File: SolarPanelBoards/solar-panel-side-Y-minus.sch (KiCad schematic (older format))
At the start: 24 parts, among them J1 Conn_01x06, U1 OPT3001DNPT

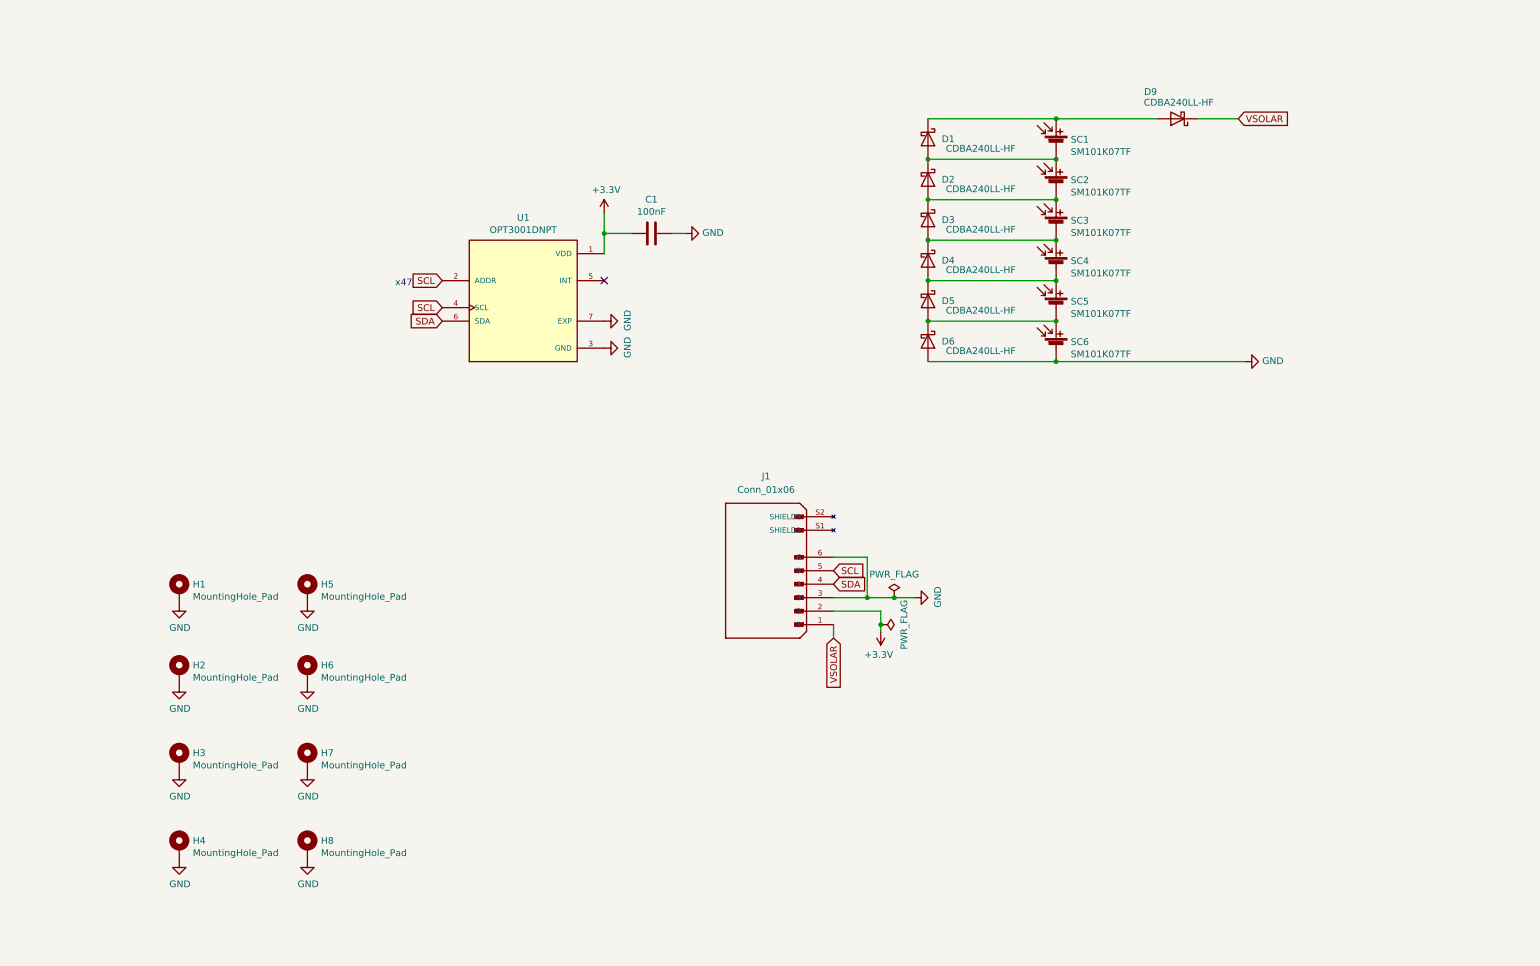
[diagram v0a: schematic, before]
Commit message: Battery board and side panels ready for CAD check and review, pycubed not finished yet
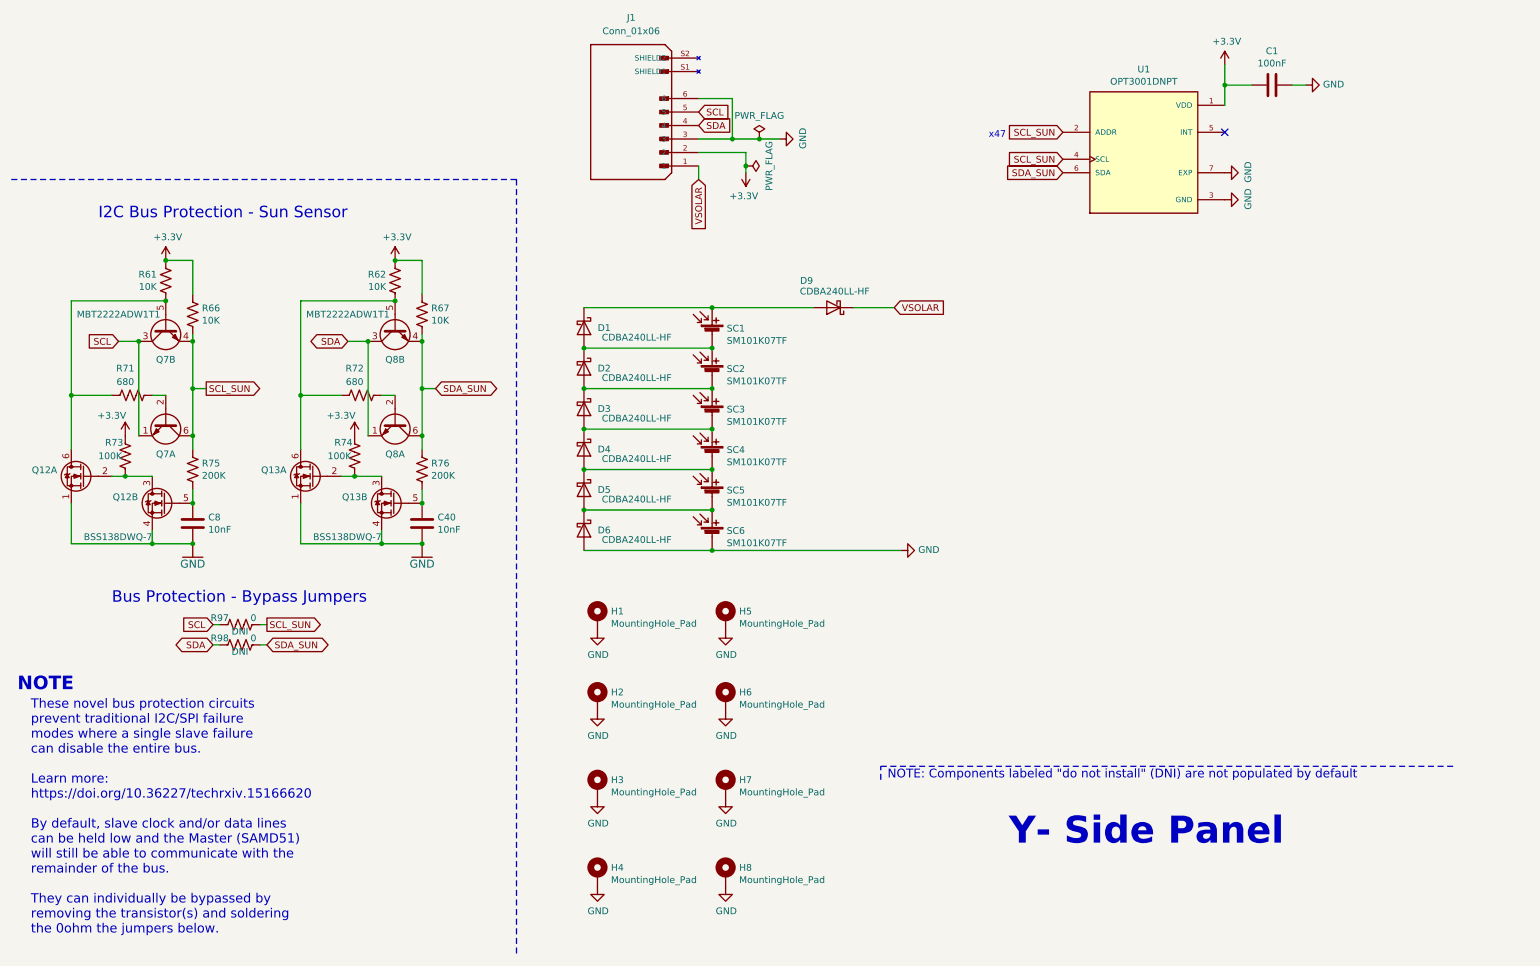
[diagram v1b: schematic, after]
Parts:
- added C40, C8: 10nF, Capacitor_SMD:C_0603_1608Metric, symbol Device:C
- added Q12, Q13: BSS138DWQ-7, sapling:BSS138DWQ-7, symbol mainboard:BSS138DWQ-7
- added Q7, Q8: MBT2222ADW1T1, Package_TO_SOT_SMD:SOT-363_SC-70-6, symbol Transistor_BJT:MBT2222ADW1T1
- added R61, R62, R66, R67: 10K, Resistor_SMD:R_0603_1608Metric, symbol Device:R_US
- added R71, R72: 680, Resistor_SMD:R_0603_1608Metric, symbol Device:R_US
- added R73, R74: 100K, Resistor_SMD:R_0603_1608Metric, symbol Device:R_US
- added R75, R76: 200K, Resistor_SMD:R_0603_1608Metric, symbol Device:R_US
- added R97, R98: 0, Resistor_SMD:R_0603_1608Metric, symbol Device:R_US
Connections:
- net +3V3: now also R61.1, R62.1, R66.1, R67.1, R73.1, R74.1
- net SCL: now also Q7.1 (E1), Q7.3 (C2), R97.2; no longer U1.2 (ADDR), U1.4 (SCL)
- net SDA: now also Q8.1 (E1), Q8.3 (C2), R98.2; no longer U1.6 (SDA)
- new net: C8.2, Q12.1 (S2), Q12.4 (S1)
- new net: Q12.2 (G2), Q12.3 (D2), R73.2
- new net: Q12.6 (D1), Q7.5 (B2), R61.2, R71.2
- new net: C8.1, Q12.5 (G1), R75.2
- new net: Q7.2 (B1), R71.1
- new net: Q8.2 (B1), R72.1
- new net: Q13.6 (D1), Q8.5 (B2), R62.2, R72.2
- new net: C40.1, Q13.5 (G1), R76.2
- new net: C40.2, Q13.1 (S2), Q13.4 (S1)
- new net: Q13.2 (G2), Q13.3 (D2), R74.2
- new net SCL_SUN: Q7.4 (E2), Q7.6 (C1), R66.2, R75.1, R97.1, U1.2 (ADDR), U1.4 (SCL)
- new net SDA_SUN: Q8.4 (E2), Q8.6 (C1), R67.2, R76.1, R98.1, U1.6 (SDA)
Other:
- note added: "Bus Protection - Bypass Jumpers"
- note added: "I2C Bus Protection - Sun Sensor"
- note added: "NOTE"
- note added: "NOTE: Components labeled "do not install" (DNI) are not populated by default"
- note added: "These novel bus protection circuits\nprevent traditional I2C/SPI failure \nmodes where a single slave failure\ncan disable the entire bus.\n\nLearn more: \nhttps://doi.org/10.36227/techrxiv.15166620\n\nBy default, slave clock and/or data lines \ncan be held low and the Master (SAMD51) \nwill still be able to communicate with the \nremainder of the bus.\n\nThey can individually be bypassed by \nre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"
- note added: "Y- Side Panel"
- moved on the sheet: C1, D4, D5, D6, H1, H2, H3, H4, H5, H6, H7, H8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
